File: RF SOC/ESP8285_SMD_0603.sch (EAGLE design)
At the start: 30 parts, among them IC1 ESP8285, Q1 600mA/40V, Q2 600mA/40V, U4 AP2112K-3.3V, Y1 CRYSTAL-26MHZSMD-3.2X2.5

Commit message: Add files via upload
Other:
- moved on the sheet: 10PF, C1, C10, C2, C8, E1, JP1, L1, L2

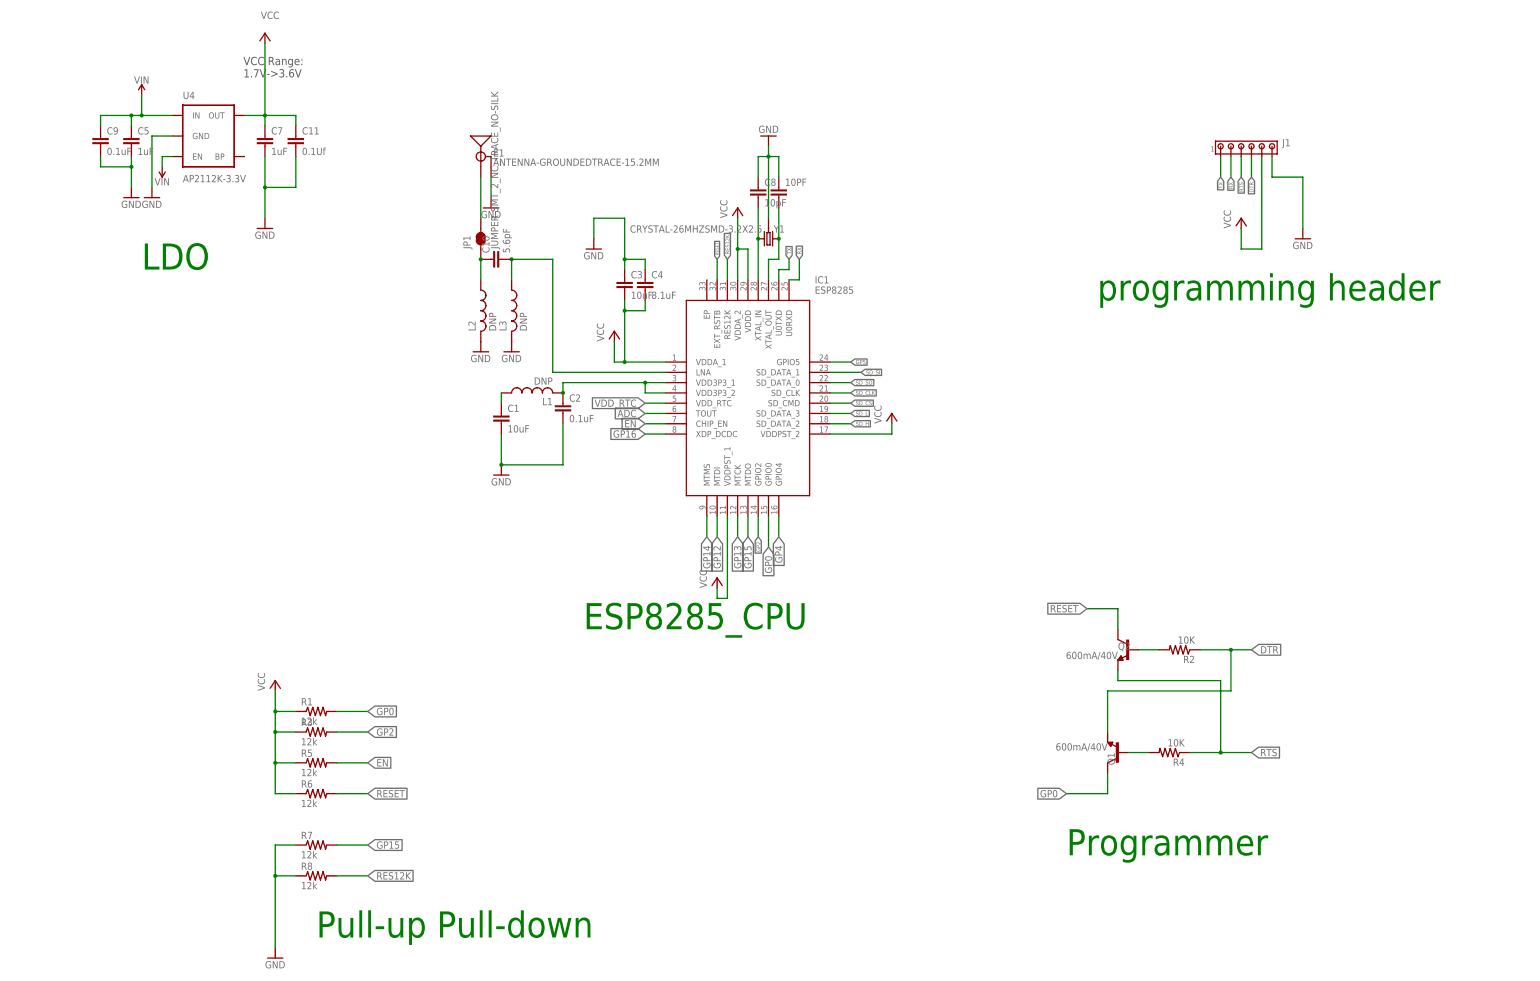
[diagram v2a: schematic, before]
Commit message: Update ESP8285_SMD_0603.sch
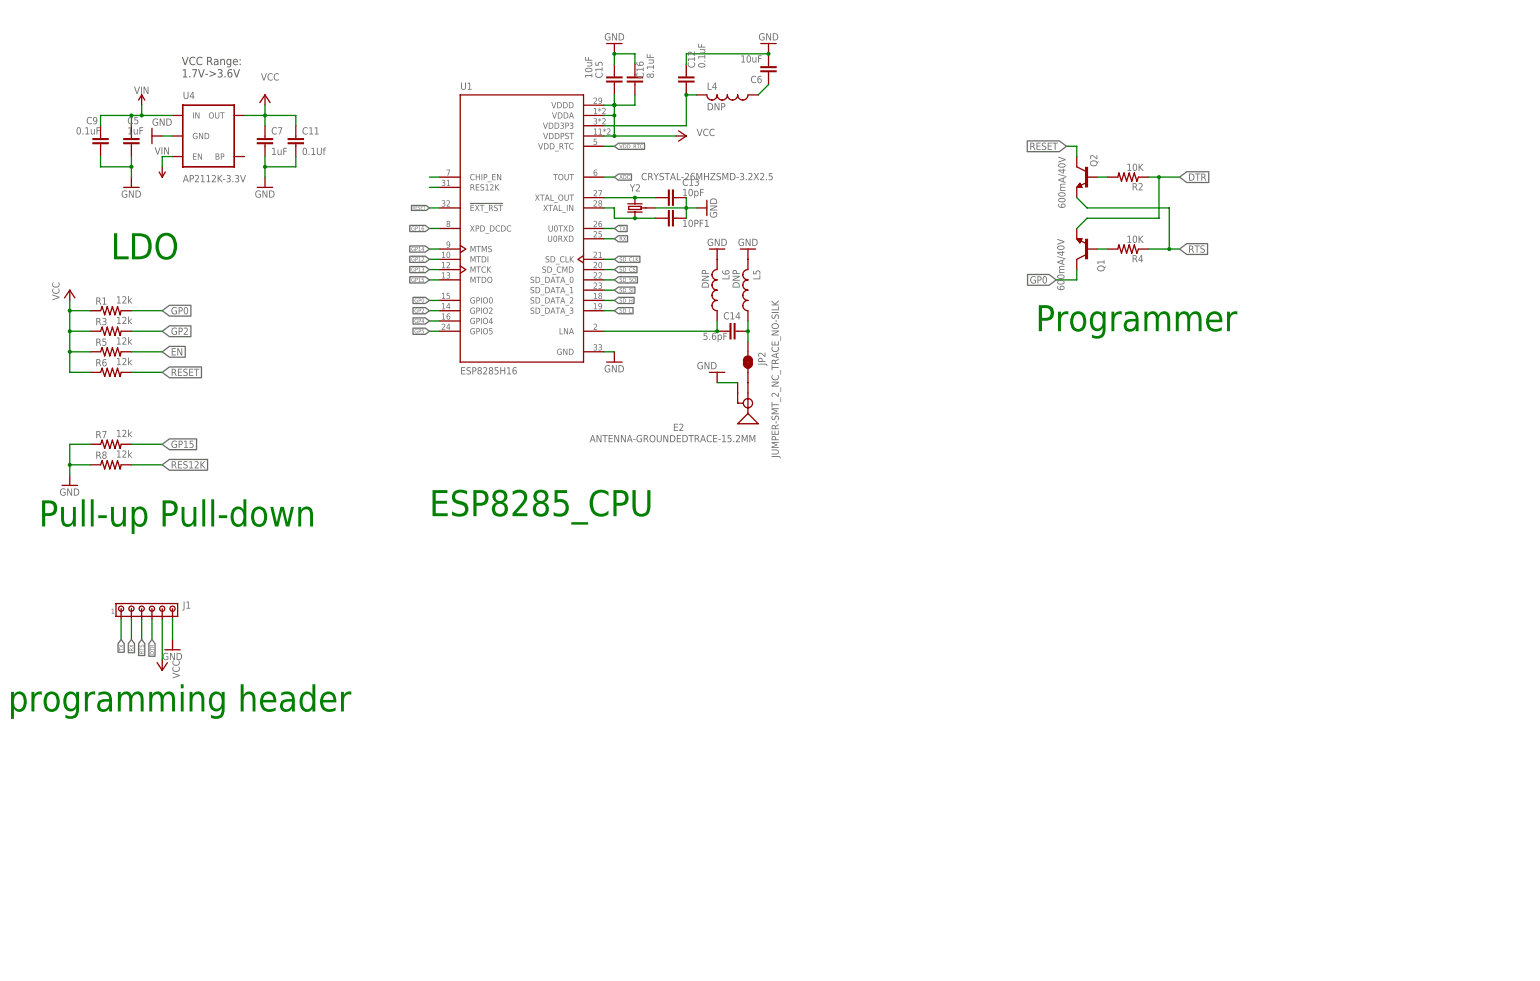
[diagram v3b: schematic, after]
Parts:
- removed 10PF: (no value), rcl:C-EUC0603
- removed C1, C3: 10uF, rcl:C-EUC0603
- removed C10: 5.6pF, rcl:C-EUC0603
- removed C2: 0.1uF, rcl:C-EUC0603
- removed C4: 8.1uF, rcl:C-EUC0603
- removed C8: 10pF, rcl:C-EUC0603
- removed E1: ANTENNA-GROUNDEDTRACE-15.2MM, SparkFun-RF:ANTENNA-GROUNDEDTRACE-15.2MM
- removed IC1: ESP8285, SamacSys_Parts:ESP8285
- removed JP1: JUMPER-SMT_2_NC_TRACE_NO-SILK, SparkFun-Jumpers:JUMPER-SMT_2_NC_TRACE_NO-SILK
- removed L1, L2, L3: DNP, rcl-2:L-USL0603
- removed Y1: CRYSTAL-26MHZSMD-3.2X2.5, SparkFun-Clocks:CRYSTAL-26MHZSMD-3.2X2.5
- added 10PF1: (no value), rcl:C-EUC0603
- added C12: 0.1uF, rcl:C-EUC0603
- added C13: 10pF, rcl:C-EUC0603
- added C14: 5.6pF, rcl:C-EUC0603
- added C15, C6: 10uF, rcl:C-EUC0603
- added C16: 8.1uF, rcl:C-EUC0603
- added E2: ANTENNA-GROUNDEDTRACE-15.2MM, SparkFun-RF:ANTENNA-GROUNDEDTRACE-15.2MM
- added JP2: JUMPER-SMT_2_NC_TRACE_NO-SILK, SparkFun-Jumpers:JUMPER-SMT_2_NC_TRACE_NO-SILK
- added L4, L5, L6: DNP, rcl-2:L-USL0603
- added U1: ESP8285H16, ESP8285H16:ESP8285H16
- added Y2: CRYSTAL-26MHZSMD-3.2X2.5, SparkFun-Clocks:CRYSTAL-26MHZSMD-3.2X2.5
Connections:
- removed net N$1: C8.2, IC1.XTAL_IN, Y1.2
- removed net N$2: C1.1, L1.1
- removed net N$3: C2.1, IC1.VDD3P3_1, IC1.VDD3P3_2, L1.2
- removed net N$4: C10.2, IC1.LNA, L3.1
- removed net N$5: C10.1, JP1.1, L2.1
- removed net N$6: E1.SIGNAL, JP1.2
- removed net N$7: 10PF.2, IC1.XTAL_OUT, Y1.1
- new net N$10: U1.CHIP_EN
- new net N$11: U1.RES12K
- new net N$12: C6.1, L4.1
- new net N$13: C12.1, L4.2, U1.VDD3P3
- new net N$23: C13.2, U1.XTAL_OUT, Y2.2
- new net N$24: C14.1, JP2.1, L5.1
- new net N$25: E2.SIGNAL, JP2.2
- new net N$26: C14.2, L6.1, U1.LNA
- new net N$29: 10PF1.2, U1.XTAL_IN, Y2.1
- net ADC: now also U1.TOUT; no longer IC1.TOUT
- net EN: no longer IC1.CHIP_EN
- net GND: now also 10PF1.1, C12.2, C13.1, C15.1, C16.1, C6.2, E2.GND, L5.2, L6.2, U1.GND, Y2.3; no longer 10PF.1, C1.2, C2.2, C3.1, C4.1, C8.1, E1.GND, L2.2, L3.2, Y1.3
- net GP0: now also U1.GPIO0; no longer IC1.GPIO0
- net GP12: now also U1.MTDI; no longer IC1.MTDI
- net GP13: now also U1.MTCK; no longer IC1.MTCK
- net GP14: now also U1.MTMS; no longer IC1.MTMS
- net GP15: now also U1.MTDO; no longer IC1.MTDO
- net GP16: now also U1.XPD_DCDC; no longer IC1.XDP_DCDC
- net GP2: now also U1.GPIO2; no longer IC1.GPIO2
- net GP4: now also U1.GPIO4; no longer IC1.GPIO4
- net GP5: now also U1.GPIO5; no longer IC1.GPIO5
- net RES12K: no longer IC1.RES12K
- net RESET: now also U1.!EXT_RST; no longer IC1.EXT_RSTB
- net RX: now also U1.U0RXD; no longer IC1.U0RXD
- net SD_CLK: now also U1.SD_CLK; no longer IC1.SD_CLK
- net SD_CS: now also U1.SD_CMD; no longer IC1.SD_CMD
- net SD_H: now also U1.SD_DATA_2; no longer IC1.SD_DATA_2
- net SD_L: now also U1.SD_DATA_3; no longer IC1.SD_DATA_3
- net SD_SI: now also U1.SD_DATA_1; no longer IC1.SD_DATA_1
- net SD_SO: now also U1.SD_DATA_0; no longer IC1.SD_DATA_0
- net TX: now also U1.U0TXD; no longer IC1.U0TXD
- net VCC: now also C15.2, C16.2, U1.VDDA, U1.VDDD, U1.VDDPST; no longer C3.2, C4.2, IC1.VDDA_1, IC1.VDDA_2, IC1.VDDD, IC1.VDDPST_1, IC1.VDDPST_2
- net VDD_RTC: now also U1.VDD_RTC; no longer IC1.VDD_RTC
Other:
- moved on the sheet: J1, Q1, Q2, R1, R2, R3, R4, R5, R6, R7, R8
